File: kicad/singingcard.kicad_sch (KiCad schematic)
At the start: 16 parts, among them J2 Audio_In, SW1 Button, U1 ISD3900FYI, U2 W25Q16JVSSIQ

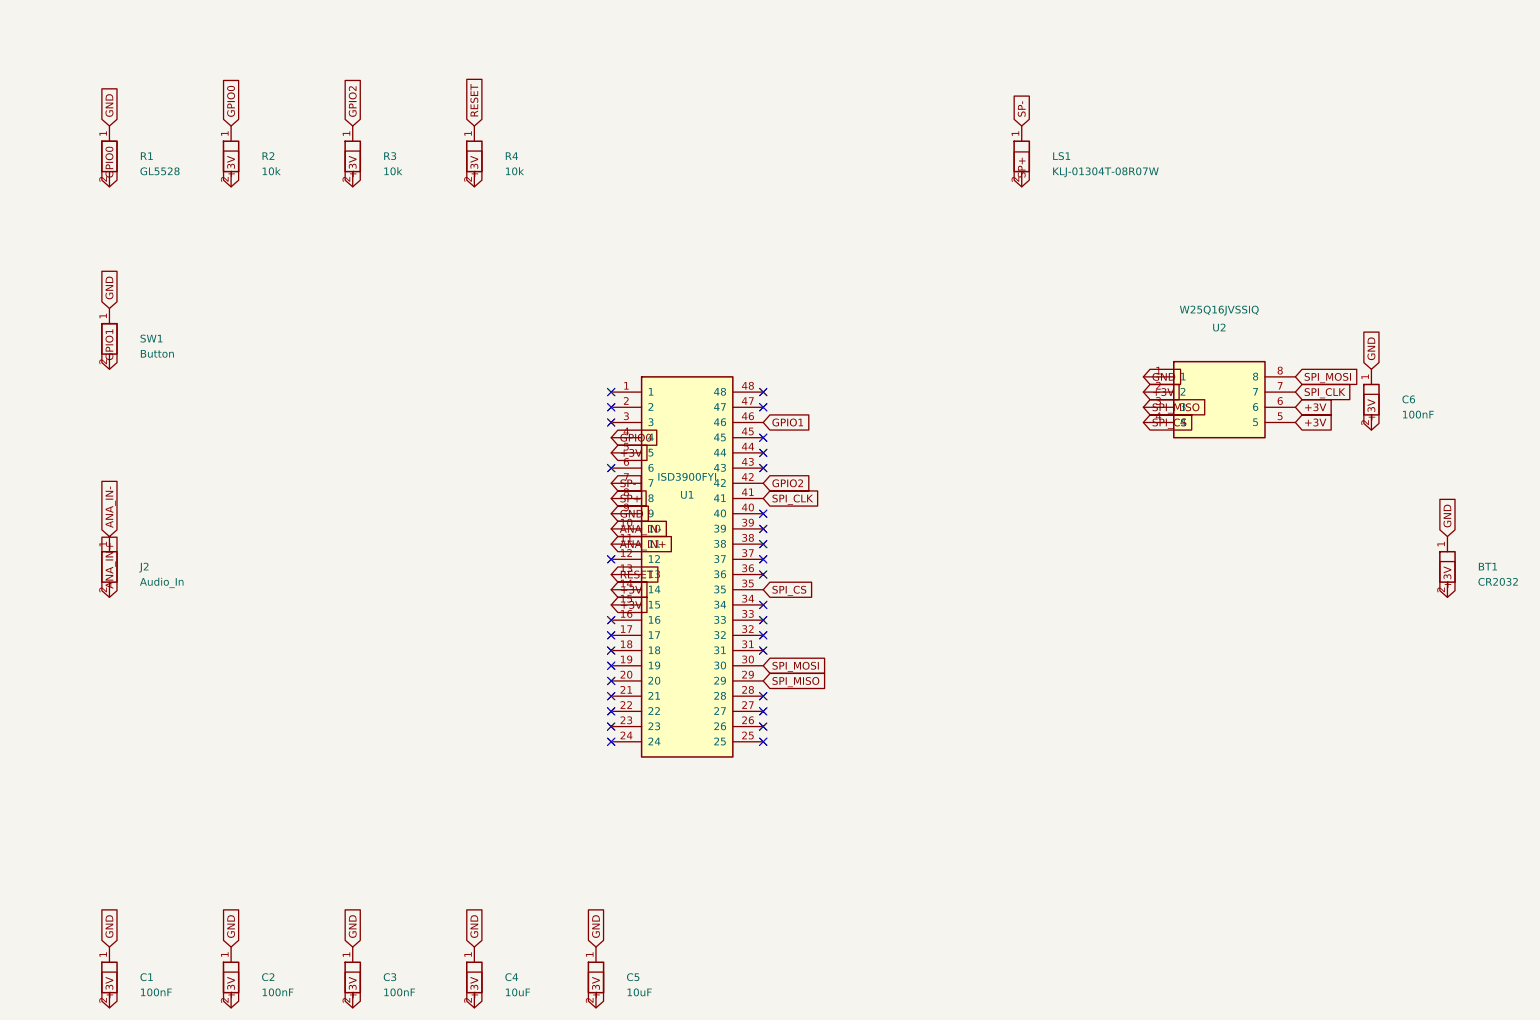
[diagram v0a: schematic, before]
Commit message: Fix global label justify and compact layout
- Fix label orientation: justify right for angles 90/180, left for 0/270
- Compact layout on A5 page (was A4)
- Move components closer together

🤖 Generated with [Claude Code](https://claude.com/claude-code)

Co-Authored-By: Claude <noreply@anthropic.com>
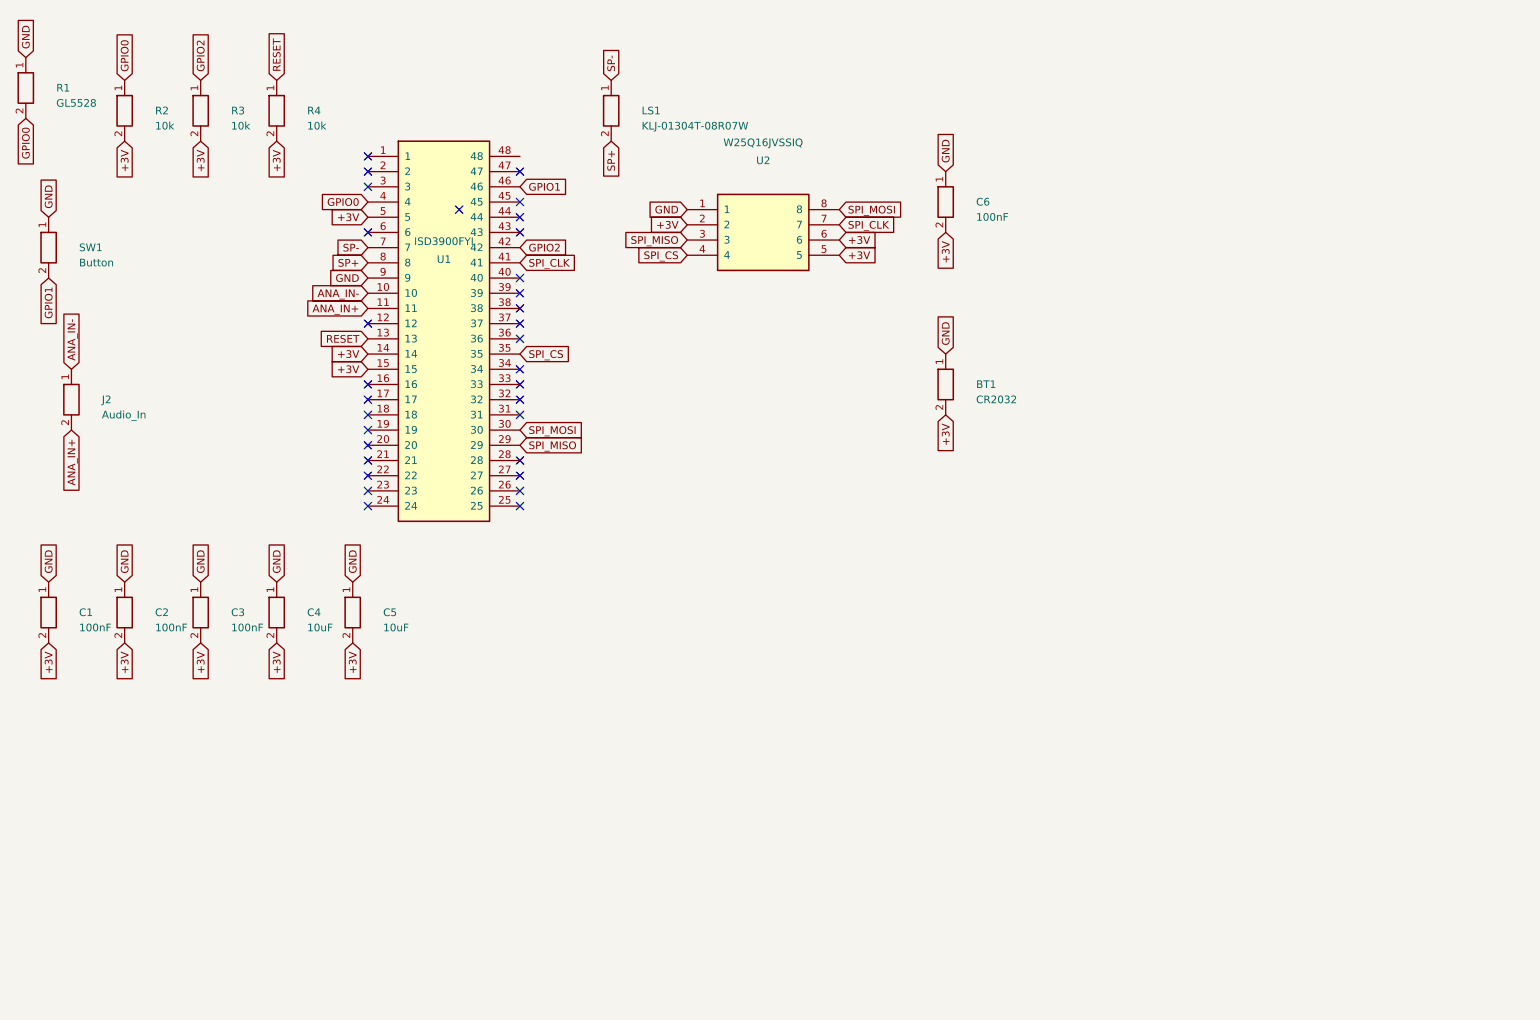
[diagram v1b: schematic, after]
